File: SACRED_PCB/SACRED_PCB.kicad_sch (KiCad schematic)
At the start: 22 parts, among them J1 Screw_Terminal_01x02, J10 Conn_01x14, J11 Conn_01x13, J2 Analog 0, J3 Analog 1, J4 Stepper 0, J5 Stepper 1, J6 Analog 2, J7 Stepper 2, J8 Stepper 3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

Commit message: Working graphing and final schematic
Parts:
- J1: footprint (none) -> TerminalBlock_MetzConnect:TerminalBlock_MetzConnect_Type011_RT05502HBWC_1x02_P5.00mm_Horizontal
- J10: footprint (none) -> Connector_PinHeader_2.54mm:PinHeader_1x14_P2.54mm_Vertical
- J11: footprint (none) -> Connector_PinHeader_2.54mm:PinHeader_1x13_P2.54mm_Vertical
- J2: footprint (none) -> Connector_JST:JST_EH_B4B-EH-A_1x04_P2.50mm_Vertical
- J4, J5, J7, J8: footprint (none) -> Connector_PinHeader_2.54mm:PinHeader_1x03_P2.54mm_Vertical
- U3: footprint (none) -> Teensy:TEENSY41
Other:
- removed sheet Analog_Channels_1
- removed sheet Analog_Channels_2
- removed sheet Analog_Channels_3
- note added: "Analog 1"
- note added: "Analog 2"
- note added: "Analog 3"

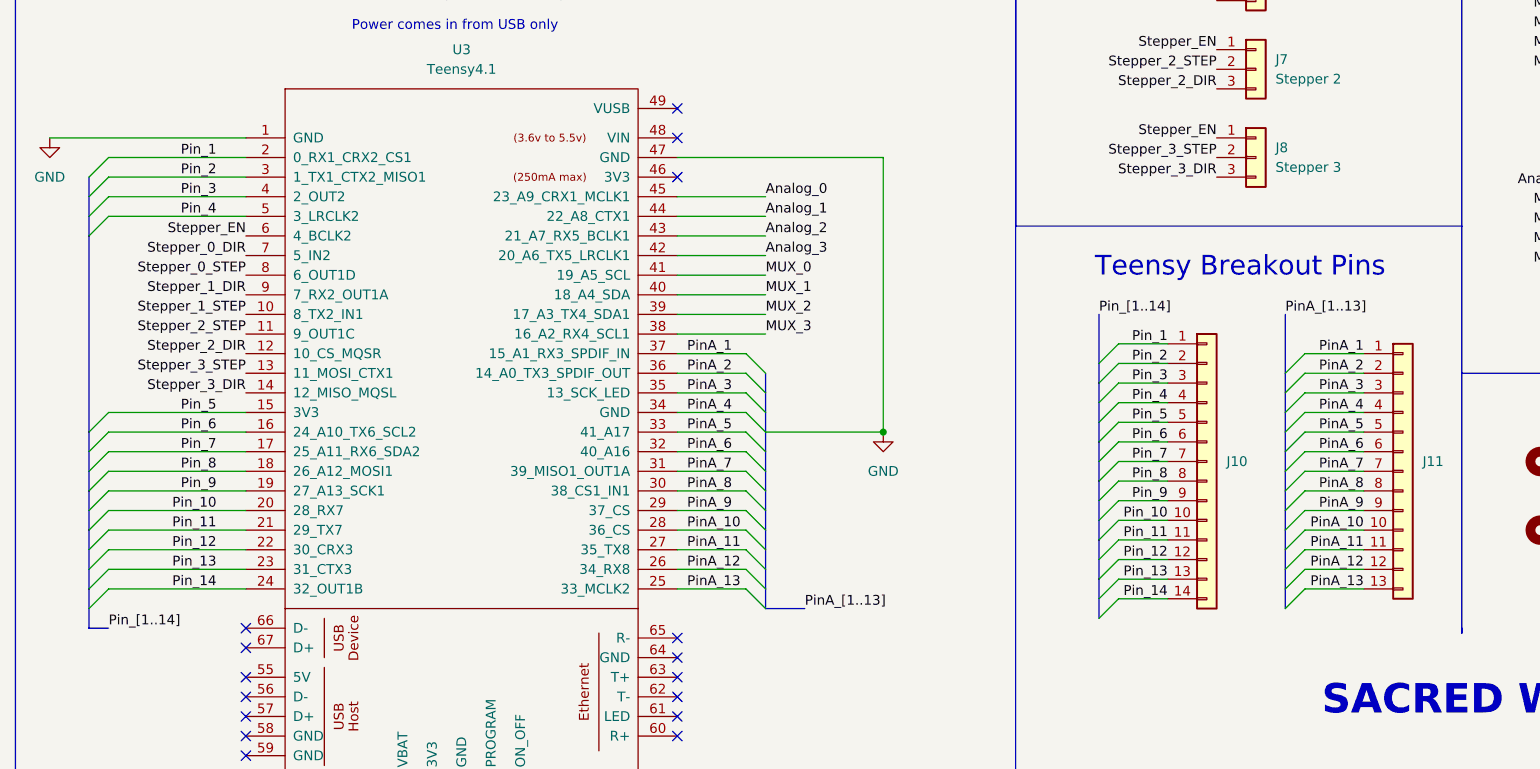
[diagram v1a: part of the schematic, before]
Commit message: Proper arm generation and PCB progress
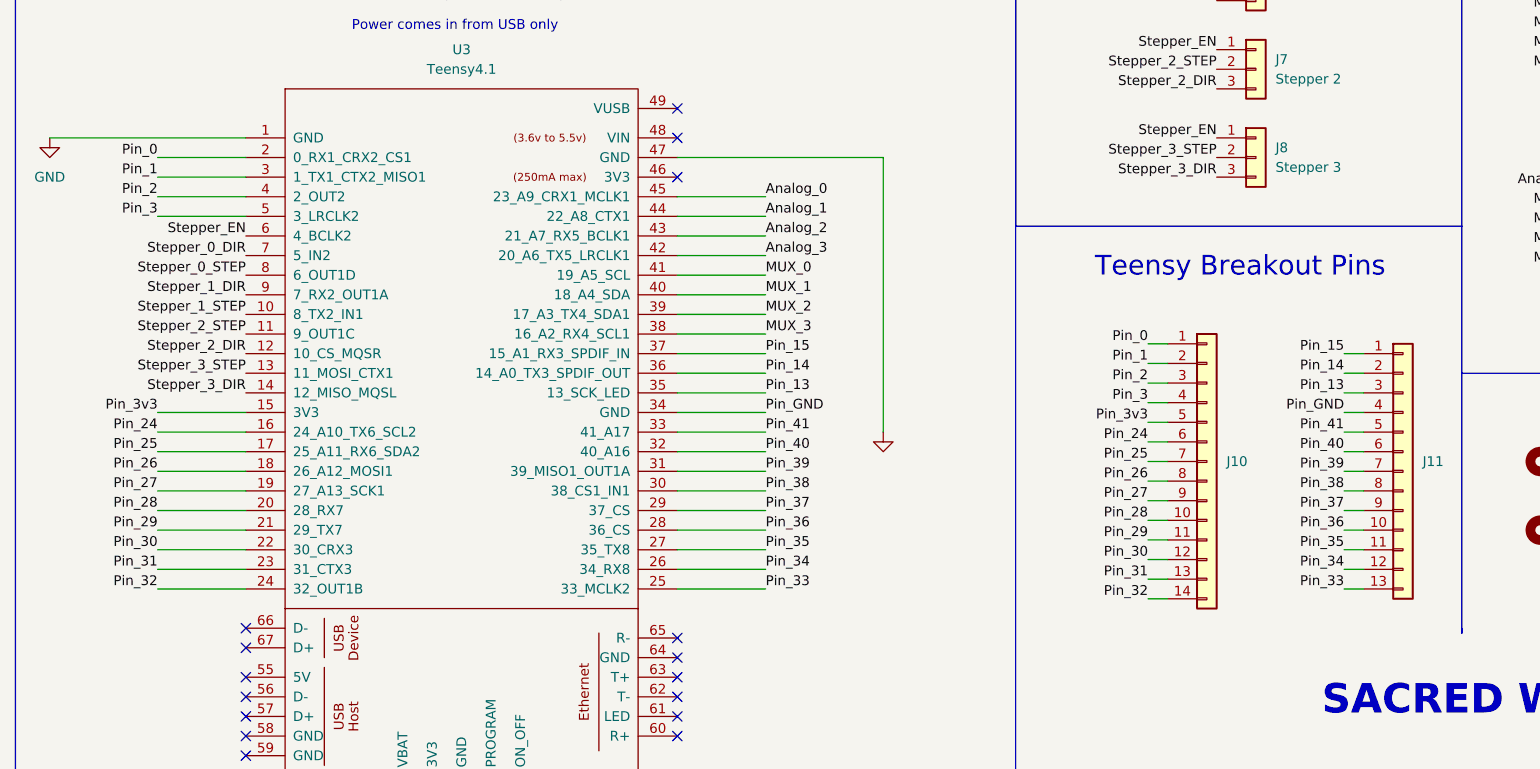
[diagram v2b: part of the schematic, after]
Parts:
- J3, J6, J9: footprint (none) -> Connector_JST:JST_EH_B4B-EH-A_1x04_P2.50mm_Vertical
- U3: footprint Teensy:TEENSY41 -> Teensy:Teensy41_2
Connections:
- net PinA_2 is gone; now on net Pin_14: J11.2 (Pin_2), U3.36 (14_A0_TX3_SPDIF_OUT)
- net PinA_3 is gone; now on net Pin_13: J11.3 (Pin_3), U3.35 (13_SCK_LED)
- net Pin_4 is gone; now on net Pin_3: J10.4 (Pin_4), U3.5 (3_LRCLK2)
- net Pin_1: now also J10.2 (Pin_2), U3.3 (1_TX1_CTX2_MISO1); no longer J10.1 (Pin_1), U3.2 (0_RX1_CRX2_CS1)
- net Pin_13: no longer J10.13 (Pin_13), U3.23 (31_CTX3)
- net Pin_14: no longer J10.14 (Pin_14), U3.24 (32_OUT1B)
- net Pin_2: now also J10.3 (Pin_3), U3.4 (2_OUT2); no longer J10.2 (Pin_2), U3.3 (1_TX1_CTX2_MISO1)
- net Pin_3: no longer J10.3 (Pin_3), U3.4 (2_OUT2)
- net PinA_1 renamed Pin_15
- net PinA_10 renamed Pin_36
- net PinA_11 renamed Pin_35
- net PinA_12 renamed Pin_34
- net PinA_13 renamed Pin_33
- net PinA_4 renamed Pin_GND
- net PinA_5 renamed Pin_41
- net PinA_6 renamed Pin_40
- net PinA_7 renamed Pin_39
- net PinA_8 renamed Pin_38
- net PinA_9 renamed Pin_37
- net Pin_10 renamed Pin_28
- net Pin_11 renamed Pin_29
- net Pin_12 renamed Pin_30
- net Pin_5 renamed Pin_3v3
- net Pin_6 renamed Pin_24
- net Pin_7 renamed Pin_25
- net Pin_8 renamed Pin_26
- net Pin_9 renamed Pin_27
- new net Pin_0: J10.1 (Pin_1), U3.2 (0_RX1_CRX2_CS1)
- new net Pin_31: J10.13 (Pin_13), U3.23 (31_CTX3)
- new net Pin_32: J10.14 (Pin_14), U3.24 (32_OUT1B)

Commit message: PCB Rev 0.1
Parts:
- removed C3, C4: 10uF, Capacitor_SMD:C_1206_3216Metric, symbol Device:C_Small
- removed U2: AMS1117-3.3, Package_TO_SOT_SMD:SOT-223-3_TabPin2, symbol Regulator_Linear:AMS1117-3.3
- added H5: MountingHole, MountingHole:MountingHole_3.2mm_M3, symbol Mechanical:MountingHole
- added J15: Screw_Terminal_01x04, TerminalBlock_Phoenix:TerminalBlock_Phoenix_MKDS-1,5-3-5.08_1x03_P5.08mm_Horizontal, symbol Connector:Screw_Terminal_01x03
- added J16: Conn_01x04, Connector_PinHeader_2.54mm:PinHeader_1x04_P2.54mm_Vertical, symbol Connector_Generic:Conn_01x04
- J1: footprint TerminalBlock_MetzConnect:TerminalBlock_MetzConnect_Type011_RT05502HBWC_1x02_P5.00mm_Horizontal -> TerminalBlock_Phoenix:TerminalBlock_Phoenix_MKDS-1,5-2_1x02_P5.00mm_Horizontal
- J10: value Conn_01x14 -> Conn_01x11; footprint Connector_PinHeader_2.54mm:PinHeader_1x14_P2.54mm_Vertical -> Connector_PinHeader_2.54mm:PinHeader_1x11_P2.54mm_Vertical; symbol Connector_Generic:Conn_01x14 -> Connector_Generic:Conn_01x11
- J2, J3, J6, J9: footprint Connector_JST:JST_EH_B4B-EH-A_1x04_P2.50mm_Vertical -> Connector_PinHeader_2.54mm:PinHeader_1x05_P2.54mm_Vertical
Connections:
- net +12V: now also J1.2 (Pin_2), J15.2 (Pin_2); no longer J1.1 (Pin_1)
- net +5V: now also J4.1 (Pin_1), J5.1 (Pin_1), J7.1 (Pin_1), J8.1 (Pin_1), J15.1 (Pin_1)
- net GND: now also J1.1 (Pin_1), J15.3 (Pin_3); no longer J1.2 (Pin_2)
- net Pin_0: now also J16.1 (Pin_1); no longer J10.1 (Pin_1)
- net Pin_1: now also J16.2 (Pin_2); no longer J10.2 (Pin_2)
- net Pin_2: now also J16.3 (Pin_3); no longer J10.3 (Pin_3)
- net Pin_24: now also J10.3 (Pin_3); no longer J10.6 (Pin_6)
- net Pin_25: now also J10.4 (Pin_4); no longer J10.7 (Pin_7)
- net Pin_26: now also J10.5 (Pin_5); no longer J10.8 (Pin_8)
- net Pin_27: now also J10.6 (Pin_6); no longer J10.9 (Pin_9)
- net Pin_28: now also J10.7 (Pin_7); no longer J10.10 (Pin_10)
- net Pin_29: now also J10.8 (Pin_8); no longer J10.11 (Pin_11)
- net Pin_3: now also J16.4 (Pin_4); no longer J10.4 (Pin_4)
- net Pin_30: now also J10.9 (Pin_9); no longer J10.12 (Pin_12)
- net Pin_31: now also J10.10 (Pin_10); no longer J10.13 (Pin_13)
- net Pin_32: now also J10.11 (Pin_11); no longer J10.14 (Pin_14)
- net Pin_3v3: now also J10.2 (Pin_2); no longer J10.5 (Pin_5)
- net Stepper_0_DIR: now also U3.13 (11_MOSI_CTX1); no longer U3.7 (5_IN2)
- net Stepper_0_STEP: now also U3.12 (10_CS_MQSR); no longer U3.8 (6_OUT1D)
- net Stepper_1_DIR: now also U3.11 (9_OUT1C); no longer U3.9 (7_RX2_OUT1A)
- net Stepper_2_DIR: now also U3.8 (6_OUT1D); no longer U3.12 (10_CS_MQSR)
- net Stepper_2_STEP: now also U3.9 (7_RX2_OUT1A); no longer U3.11 (9_OUT1C)
- net Stepper_3_DIR: now also U3.6 (4_BCLK2); no longer U3.14 (12_MISO_MQSL)
- net Stepper_3_STEP: now also U3.7 (5_IN2); no longer U3.13 (11_MOSI_CTX1)
- removed net Stepper_EN: J4.1 (Pin_1), J5.1 (Pin_1), J7.1 (Pin_1), J8.1 (Pin_1), U3.6 (4_BCLK2)
- new net Pin_12: J10.1 (Pin_1), U3.14 (12_MISO_MQSL)
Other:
- note added: "Power output from main board"
- note removed: "3.3V Regulator"
- moved on the sheet: J11, J4, J5, J7, J8
